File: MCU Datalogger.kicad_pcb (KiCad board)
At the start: 2 copper layers, 29 parts, among them J1 Conn_01x04_Pin, J2 Conn_01x04_Pin, J3 Conn_01x09_Pin, J4 Conn_02x03_Odd_Even, U1 24LC1025, U2 24LC1025, U3 DS1337S_, U4 ATMEGA328P-AU, Y1 16 MHz, Y2 32.768 KHz

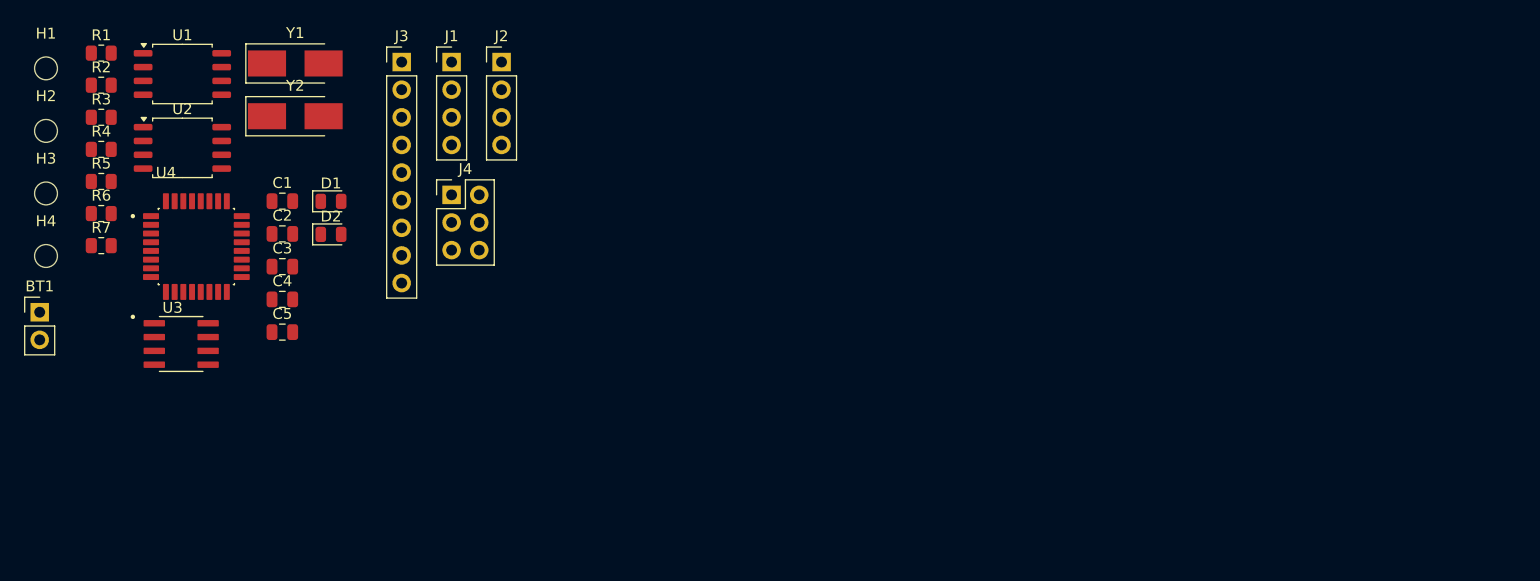
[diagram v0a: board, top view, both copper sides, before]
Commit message: Completed placement of footprints.
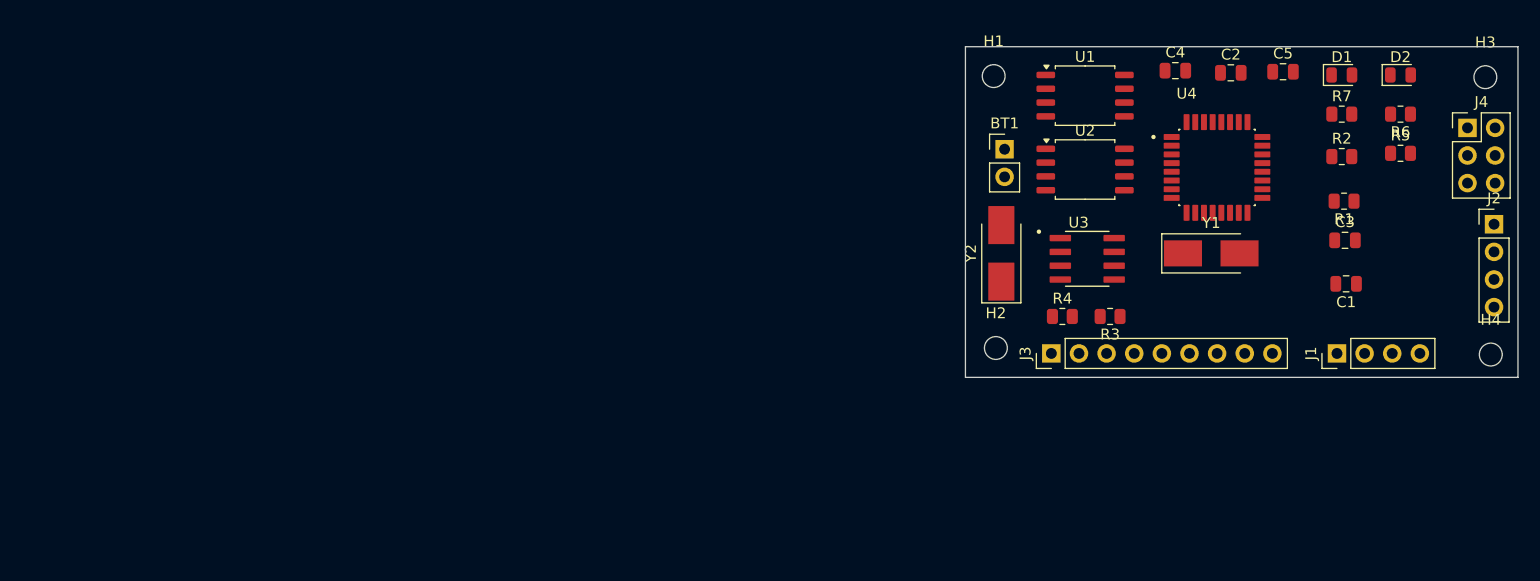
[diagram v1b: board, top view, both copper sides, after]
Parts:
- moved H4 133.1 mm to (197.5, 89.4)
- moved H3 132.8 mm to (197.0, 63.9)
- moved R6 119.8 mm to (189.2, 67.3), turned to 180 degrees
- moved R5 119.5 mm to (189.2, 70.9)
- moved R1 115.1 mm to (184.0, 75.3), turned to 180 degrees
- moved R7 114.7 mm to (183.8, 67.3)
- moved R2 114.2 mm to (183.8, 71.2)
- moved D2 99.4 mm to (189.2, 63.7)
- moved C1 98.1 mm to (184.2, 82.9), turned to 180 degrees
- moved C3 97.7 mm to (184.1, 78.9)
- moved C5 95.1 mm to (178.4, 63.4)
- moved R3 94.5 mm to (162.5, 85.9), turned to 180 degrees
- moved U4 94.1 mm to (172.3, 72.2)
- moved D1 93.7 mm to (183.8, 63.7)
- moved J4 93.6 mm to (195.4, 68.6)
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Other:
- board outline added: 50.8 x 30.4 mm

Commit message: Routing sans GND Vcc complete.
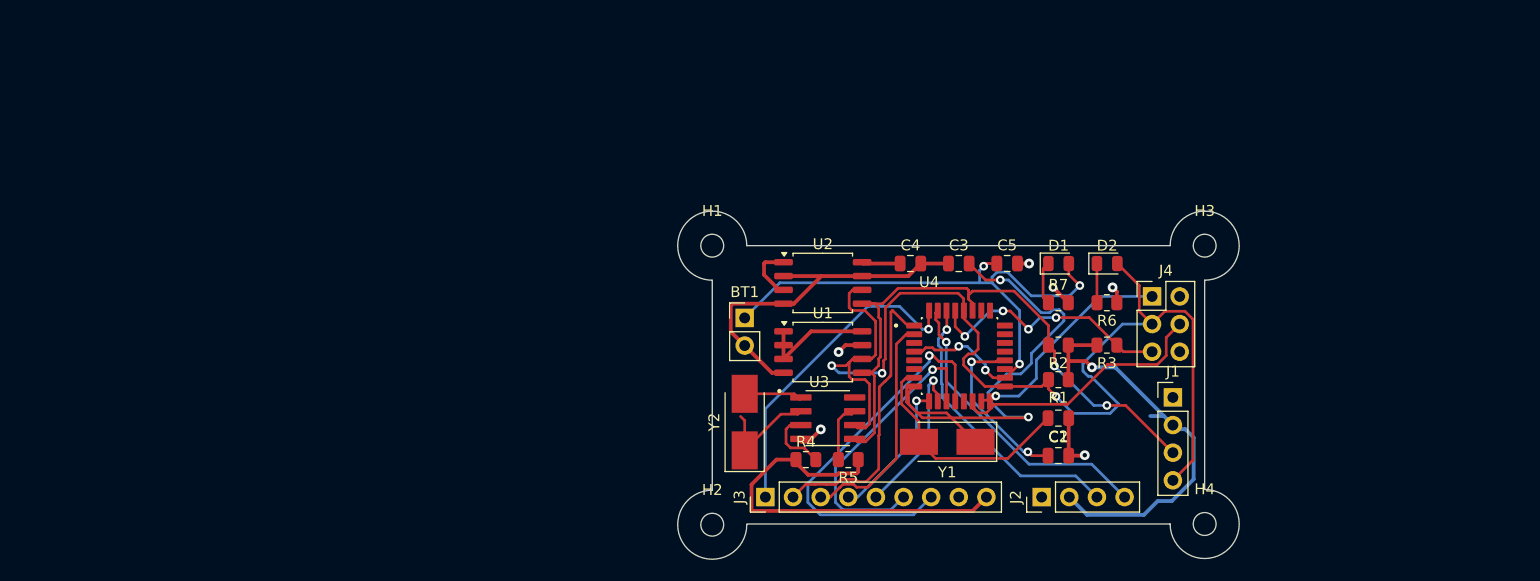
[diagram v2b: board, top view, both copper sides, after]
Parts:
- moved R5 58.1 mm to (138.4, 99.1), turned to 180 degrees
- moved J2 48.6 mm to (156.2, 102.5), turned to 90 degrees
- moved C3 35.6 mm to (148.6, 81.0)
- moved C2 35.5 mm to (157.7, 95.2), turned to 180 degrees
- moved U1 33.7 mm to (136.1, 89.2)
- moved J4 32.9 mm to (166.4, 84.1)
- moved R6 32.1 mm to (162.2, 84.6)
- moved D2 32.1 mm to (162.2, 81.0)
- moved R7 31.3 mm to (157.7, 84.6)
- moved R2 31.3 mm to (157.7, 88.5), turned to 180 degrees
- moved D1 31.3 mm to (157.8, 81.0)
- moved R1 31.0 mm to (157.7, 91.7)
- moved C5 30.9 mm to (153.0, 81.0)
- moved C1 30.8 mm to (157.7, 98.7), turned to 0 degrees
- moved H2 30.7 mm to (125.9, 105.0)
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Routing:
- net /SCK: track 0.00 -> 106.7 mm, vias 0 -> 3
- net /Vcc: track 0.00 -> 95.3 mm, vias 0 -> 1
- net Net-(BT1-+): track 0.00 -> 60.1 mm, vias 0 -> 5
- net /SDA: track 0.00 -> 56.6 mm, vias 0 -> 2
- net Net-(U4-PB7): track 0.00 -> 50.1 mm, vias 0 -> 2
- net GND: track 0.00 -> 48.7 mm, vias 0 -> 6
- net /D8: track 0.00 -> 36.7 mm, vias 0 -> 1
- net /D2: track 0.00 -> 29.6 mm, vias 0 -> 1
- net /TX: track 0.00 -> 27.9 mm, vias 0 -> 1
- net /D7: track 0.00 -> 27.3 mm, vias 0 -> 1
- net /D3: track 0.00 -> 26.8 mm
- net /RX: track 0.00 -> 26.5 mm, vias 0 -> 1
- net /MOSI: track 0.00 -> 24.1 mm
- net /RESET: track 0.00 -> 23.3 mm, vias 0 -> 4
- net Net-(U4-PB6): track 0.00 -> 21.5 mm
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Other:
- board size 50.8 x 30.4 mm -> 51.6 x 32 mm

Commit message: Add files via upload
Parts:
- added G***: LOGO, Breadboard Power Supply:TMFR, B.Cu at (147.5, 97.5)
- moved Y1 0.70 mm to (148.2, 97.4)
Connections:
- BT1 pad 1: Net-(BT1-+) -> /Vcc
- C5 pad 1: Net-(BT1-+) -> /Vcc
- D1 pad 2: Net-(BT1-+) -> /Vcc
- J1 pad 4: /SCK -> /SCL
- R1 pad 2: /SCK -> /SCL
- U1 pad 6: /SCK -> /SCL
- U2 pad 6: /SCK -> /SCL
- U3 pad 6: /SCK -> /SCL
- U4 pad 18: Net-(BT1-+) -> /Vcc
- U4 pad 28: /SCK -> /SCL
- U4 pad 4: Net-(BT1-+) -> /Vcc
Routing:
- net /SCK: track 106.7 -> 23.7 mm, vias 3 -> 1
- net /SCL: track 0.00 -> 66.2 mm, vias 0 -> 4
- net Net-(BT1-+): track 60.1 -> 0.00 mm, vias 5 -> 0
- net /Vcc: track 95.3 -> 43.3 mm, vias 1 -> 13
- net Net-(U4-PB7): track 50.1 -> 23.1 mm, vias 2 -> 3
- net /D8: track 36.7 -> 17.7 mm, vias 1 -> 0
- net /D7: track 27.3 -> 11.8 mm, vias 1 -> 0
- net /SDA: track 56.6 -> 51.4 mm, vias 2 -> 5
- net /TX: track 27.9 -> 32.9 mm, vias 1 -> 0
- net Net-(U3-X2): track 9.93 -> 6.65 mm
- net /RX: track 26.5 -> 29.3 mm, vias 1 -> 0
- net GND: track 48.7 -> 46.0 mm, vias 6 -> 11
- net /D3: track 26.8 -> 24.3 mm
- net /MOSI: track 24.1 -> 26.5 mm, vias 0 -> 2
- net /D6: track 15.0 -> 13.0 mm, vias 1 -> 0
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- added copper zone on In2.Cu, net /Vcc
- added copper zone on B.Cu, net GND
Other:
- copper layers 2 -> 4
- board text added: "- 2Mbit EEPROM - RTC - 12C, SPI, GPIOs"
- board text added: "Data logger with the ATMega328P."
- board text added: "ICSP MISO | VCC SCK | MOSI RESET| GND"
